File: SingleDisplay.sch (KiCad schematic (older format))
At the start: 5 parts, among them U2 MAX7221, U3 5x7Segment

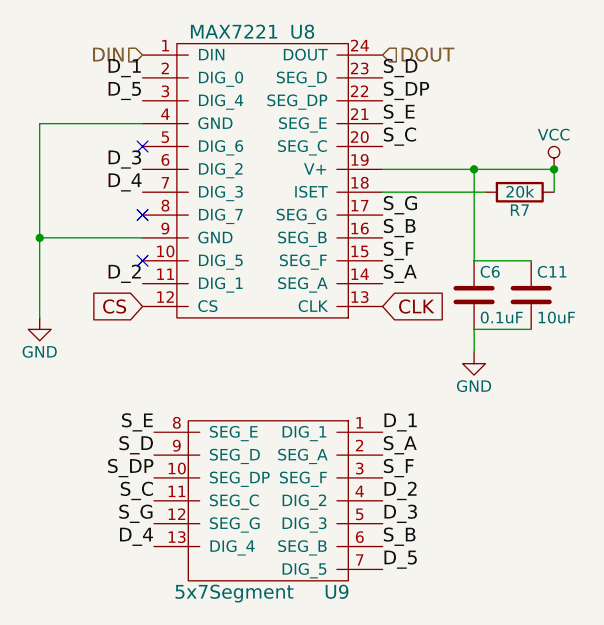
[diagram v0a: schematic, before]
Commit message: Finished trace routing.  Added 3d parts
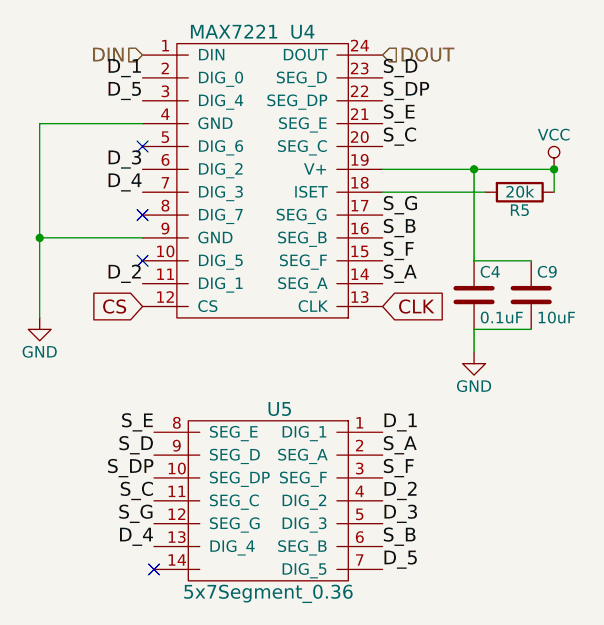
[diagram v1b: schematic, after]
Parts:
- removed U3: 5x7Segment, custom:5x7Segment, symbol 5x7Segment
- added U3: 5x7Segment_0.36, custom:5x7Segment_0.36, symbol 5x7Segment_0.36
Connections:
- net D_1: now also U3.1 (DIG_1)
- net D_2: now also U3.4 (DIG_2)
- net D_3: now also U3.5 (DIG_3)
- net D_4: now also U3.13 (DIG_4)
- net D_5: now also U3.7 (DIG_5)
- net S_A: now also U3.2 (SEG_A)
- net S_B: now also U3.6 (SEG_B)
- net S_C: now also U3.11 (SEG_C)
- net S_D: now also U3.9 (SEG_D)
- net S_DP: now also U3.10 (SEG_DP)
- net S_E: now also U3.8 (SEG_E)
- net S_F: now also U3.3 (SEG_F)
- net S_G: now also U3.12 (SEG_G)
- no-connect marks 3 -> 4
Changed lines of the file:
@@
 $Descr A4 11693 8268
 encoding utf-8
-Sheet 5 5
+Sheet 4 5
 Title ""
 Date ""
@@
 AR Path="/59D41D61/59D40956" Ref="R6"  Part="1"
 AR Path="/59D41D65/59D40956" Ref="R7"  Part="1"
-F 0 "R7" V 6480 3000 50  0000 C CNN
+F 0 "R5" V 6480 3000 50  0000 C CNN
 F 1 "20k" V 6400 3000 50  0000 C CNN
 F 2 "Resistors_SMD:R_0805" V 6330 3000 50  0001 C CNN
@@
 $EndComp
 $Comp
-L GND #PWR028
+L GND #PWR031
 U 1 1 59D4095E
 P 4300 3550
-AR Path="/59D40580/59D4095E" Ref="#PWR028"  Part="1"
-AR Path="/59D412E4/59D4095E" Ref="#PWR031"  Part="1"
-AR Path="/59D41D61/59D4095E" Ref="#PWR034"  Part="1"
-AR Path="/59D41D65/59D4095E" Ref="#PWR037"  Part="1"
-F 0 "#PWR037" H 4300 3300 50  0001 C CNN
+AR Path="/59D40580/59D4095E" Ref="#PWR031"  Part="1"
+AR Path="/59D412E4/59D4095E" Ref="#PWR034"  Part="1"
+AR Path="/59D41D61/59D4095E" Ref="#PWR037"  Part="1"
+AR Path="/59D41D65/59D4095E" Ref="#PWR040"  Part="1"
+F 0 "#PWR040" H 4300 3300 50  0001 C CNN
 F 1 "GND" H 4300 3400 50  0000 C CNN
 F 2 "" H 4300 3550 50  0000 C CNN
@@
 $EndComp
 $Comp
-L GND #PWR029
+L GND #PWR032
 U 1 1 59D40964
 P 6200 3700
-AR Path="/59D40580/59D40964" Ref="#PWR029"  Part="1"
-AR Path="/59D412E4/59D40964" Ref="#PWR032"  Part="1"
-AR Path="/59D41D61/59D40964" Ref="#PWR035"  Part="1"
-AR Path="/59D41D65/59D40964" Ref="#PWR038"  Part="1"
-F 0 "#PWR038" H 6200 3450 50  0001 C CNN
+AR Path="/59D40580/59D40964" Ref="#PWR032"  Part="1"
+AR Path="/59D412E4/59D40964" Ref="#PWR035"  Part="1"
+AR Path="/59D41D61/59D40964" Ref="#PWR038"  Part="1"
+AR Path="/59D41D65/59D40964" Ref="#PWR041"  Part="1"
+F 0 "#PWR041" H 6200 3450 50  0001 C CNN
 F 1 "GND" H 6200 3550 50  0000 C CNN
 F 2 "" H 6200 3700 50  0000 C CNN
@@
 AR Path="/59D41D61/59D4096A" Ref="C5"  Part="1"
 AR Path="/59D41D65/59D4096A" Ref="C6"  Part="1"
-F 0 "C6" H 6225 3550 50  0000 L CNN
+F 0 "C4" H 6225 3550 50  0000 L CNN
 F 1 "0.1uF" H 6225 3350 50  0000 L CNN
 F 2 "Capacitors_SMD:C_0805" H 6238 3300 50  0001 C CNN
@@
 AR Path="/59D41D61/59D40971" Ref="C10"  Part="1"
 AR Path="/59D41D65/59D40971" Ref="C11"  Part="1"
-F 0 "C11" H 6475 3550 50  0000 L CNN
+F 0 "C9" H 6475 3550 50  0000 L CNN
 F 1 "10uF" H 6475 3350 50  0000 L CNN
 F 2 "Capacitors_SMD:C_0805" H 6488 3300 50  0001 C CNN
@@
 AR Path="/59D41D61/59D40980" Ref="U6"  Part="1"
 AR Path="/59D41D65/59D40980" Ref="U8"  Part="1"
-F 0 "U8" H 5450 3500 60  0000 C CNN
+F 0 "U4" H 5450 3500 60  0000 C CNN
 F 1 "MAX7221" H 5150 3500 60  0000 C CNN
 F 2 "custom:MAX7221CWG" H 5300 2900 60  0001 C CNN
@@
 $EndComp
 $Comp
-L VCC #PWR030
+L VCC #PWR033
 U 1 1 59D40987
 P 6550 2900
-AR Path="/59D40580/59D40987" Ref="#PWR030"  Part="1"
-AR Path="/59D412E4/59D40987" Ref="#PWR033"  Part="1"
-AR Path="/59D41D61/59D40987" Ref="#PWR036"  Part="1"
-AR Path="/59D41D65/59D40987" Ref="#PWR039"  Part="1"
-F 0 "#PWR039" H 6550 2750 50  0001 C CNN
+AR Path="/59D40580/59D40987" Ref="#PWR033"  Part="1"
+AR Path="/59D412E4/59D40987" Ref="#PWR036"  Part="1"
+AR Path="/59D41D61/59D40987" Ref="#PWR039"  Part="1"
+AR Path="/59D41D65/59D40987" Ref="#PWR042"  Part="1"
+F 0 "#PWR042" H 6550 2750 50  0001 C CNN
 F 1 "VCC" H 6550 3050 50  0000 C CNN
 F 2 "" H 6550 2900 50  0000 C CNN
@@
 CS
 $Comp
-L 5x7Segment U3
-U 1 1 59DAB88D
+L 5x7Segment_0.36 U3
+U 1 1 59EA5343
 P 5350 4300
-AR Path="/59D40580/59DAB88D" Ref="U3"  Part="1"
-AR Path="/59D412E4/59DAB88D" Ref="U5"  Part="1"
-AR Path="/59D41D61/59DAB88D" Ref="U7"  Part="1"
-AR Path="/59D41D65/59DAB88D" Ref="U9"  Part="1"
-F 0 "U9" V 5800 4550 60  0000 C CNN
-F 1 "5x7Segment" V 5800 4100 60  0000 C CNN
-F 2 "custom:5x7Segment" H 5600 4400 60  0001 C CNN
+AR Path="/59D40580/59EA5343" Ref="U3"  Part="1"
+AR Path="/59D412E4/59EA5343" Ref="U5"  Part="1"
+AR Path="/59D41D61/59EA5343" Ref="U7"  Part="1"
+AR Path="/59D41D65/59EA5343" Ref="U9"  Part="1"
+F 0 "U5" V 5000 4300 60  0000 C CNN
+F 1 "5x7Segment_0.36" V 5800 4250 60  0000 C CNN
+F 2 "custom:5x7Segment_0.36" H 5600 4400 60  0001 C CNN
 F 3 "" H 5600 4400 60  0001 C CNN
 	1    5350 4300
 	0    1    1    0
 $EndComp
+NoConn ~ 4800 4650
 $EndSCHEMATC

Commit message: Tons of updates.  Mostly working.
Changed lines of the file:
@@
 EESchema Schematic File Version 2
+LIBS:display-rescue
 LIBS:power
 LIBS:device
@@
 $Descr A4 11693 8268
 encoding utf-8
-Sheet 4 5
+Sheet 2 5
 Title ""
 Date ""
@@
 AR Path="/59D41D61/59D40956" Ref="R6"  Part="1"
 AR Path="/59D41D65/59D40956" Ref="R7"  Part="1"
-F 0 "R5" V 6480 3000 50  0000 C CNN
+F 0 "R4" V 6480 3000 50  0000 C CNN
 F 1 "20k" V 6400 3000 50  0000 C CNN
 F 2 "Resistors_SMD:R_0805" V 6330 3000 50  0001 C CNN
@@
 $EndComp
 $Comp
-L GND #PWR031
+L GND #PWR033
 U 1 1 59D4095E
 P 4300 3550
-AR Path="/59D40580/59D4095E" Ref="#PWR031"  Part="1"
-AR Path="/59D412E4/59D4095E" Ref="#PWR034"  Part="1"
-AR Path="/59D41D61/59D4095E" Ref="#PWR037"  Part="1"
-AR Path="/59D41D65/59D4095E" Ref="#PWR040"  Part="1"
-F 0 "#PWR040" H 4300 3300 50  0001 C CNN
+AR Path="/59D40580/59D4095E" Ref="#PWR033"  Part="1"
+AR Path="/59D412E4/59D4095E" Ref="#PWR036"  Part="1"
+AR Path="/59D41D61/59D4095E" Ref="#PWR039"  Part="1"
+AR Path="/59D41D65/59D4095E" Ref="#PWR042"  Part="1"
+F 0 "#PWR033" H 4300 3300 50  0001 C CNN
 F 1 "GND" H 4300 3400 50  0000 C CNN
 F 2 "" H 4300 3550 50  0000 C CNN
@@
 $EndComp
 $Comp
-L GND #PWR032
+L GND #PWR034
 U 1 1 59D40964
 P 6200 3700
-AR Path="/59D40580/59D40964" Ref="#PWR032"  Part="1"
-AR Path="/59D412E4/59D40964" Ref="#PWR035"  Part="1"
-AR Path="/59D41D61/59D40964" Ref="#PWR038"  Part="1"
-AR Path="/59D41D65/59D40964" Ref="#PWR041"  Part="1"
-F 0 "#PWR041" H 6200 3450 50  0001 C CNN
+AR Path="/59D40580/59D40964" Ref="#PWR034"  Part="1"
+AR Path="/59D412E4/59D40964" Ref="#PWR037"  Part="1"
+AR Path="/59D41D61/59D40964" Ref="#PWR040"  Part="1"
+AR Path="/59D41D65/59D40964" Ref="#PWR043"  Part="1"
+F 0 "#PWR034" H 6200 3450 50  0001 C CNN
 F 1 "GND" H 6200 3550 50  0000 C CNN
 F 2 "" H 6200 3700 50  0000 C CNN
@@
 AR Path="/59D41D61/59D4096A" Ref="C5"  Part="1"
 AR Path="/59D41D65/59D4096A" Ref="C6"  Part="1"
-F 0 "C4" H 6225 3550 50  0000 L CNN
+F 0 "C3" H 6225 3550 50  0000 L CNN
 F 1 "0.1uF" H 6225 3350 50  0000 L CNN
 F 2 "Capacitors_SMD:C_0805" H 6238 3300 50  0001 C CNN
@@
 AR Path="/59D41D61/59D40971" Ref="C10"  Part="1"
 AR Path="/59D41D65/59D40971" Ref="C11"  Part="1"
-F 0 "C9" H 6475 3550 50  0000 L CNN
+F 0 "C8" H 6475 3550 50  0000 L CNN
 F 1 "10uF" H 6475 3350 50  0000 L CNN
 F 2 "Capacitors_SMD:C_0805" H 6488 3300 50  0001 C CNN
@@
 AR Path="/59D41D61/59D40980" Ref="U6"  Part="1"
 AR Path="/59D41D65/59D40980" Ref="U8"  Part="1"
-F 0 "U4" H 5450 3500 60  0000 C CNN
+F 0 "U2" H 5450 3500 60  0000 C CNN
 F 1 "MAX7221" H 5150 3500 60  0000 C CNN
 F 2 "custom:MAX7221CWG" H 5300 2900 60  0001 C CNN
@@
 $EndComp
 $Comp
-L VCC #PWR033
+L VCC #PWR035
 U 1 1 59D40987
 P 6550 2900
-AR Path="/59D40580/59D40987" Ref="#PWR033"  Part="1"
-AR Path="/59D412E4/59D40987" Ref="#PWR036"  Part="1"
-AR Path="/59D41D61/59D40987" Ref="#PWR039"  Part="1"
-AR Path="/59D41D65/59D40987" Ref="#PWR042"  Part="1"
-F 0 "#PWR042" H 6550 2750 50  0001 C CNN
+AR Path="/59D40580/59D40987" Ref="#PWR035"  Part="1"
+AR Path="/59D412E4/59D40987" Ref="#PWR038"  Part="1"
+AR Path="/59D41D61/59D40987" Ref="#PWR041"  Part="1"
+AR Path="/59D41D65/59D40987" Ref="#PWR044"  Part="1"
+F 0 "#PWR035" H 6550 2750 50  0001 C CNN
 F 1 "VCC" H 6550 3050 50  0000 C CNN
 F 2 "" H 6550 2900 50  0000 C CNN
@@
 AR Path="/59D41D61/59EA5343" Ref="U7"  Part="1"
 AR Path="/59D41D65/59EA5343" Ref="U9"  Part="1"
-F 0 "U5" V 5000 4300 60  0000 C CNN
+F 0 "U3" V 5000 4300 60  0000 C CNN
 F 1 "5x7Segment_0.36" V 5800 4250 60  0000 C CNN
 F 2 "custom:5x7Segment_0.36" H 5600 4400 60  0001 C CNN
